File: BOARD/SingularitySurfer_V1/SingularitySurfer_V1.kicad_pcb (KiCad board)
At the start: 2 copper layers, 99.1 x 68.6 mm, 0 parts

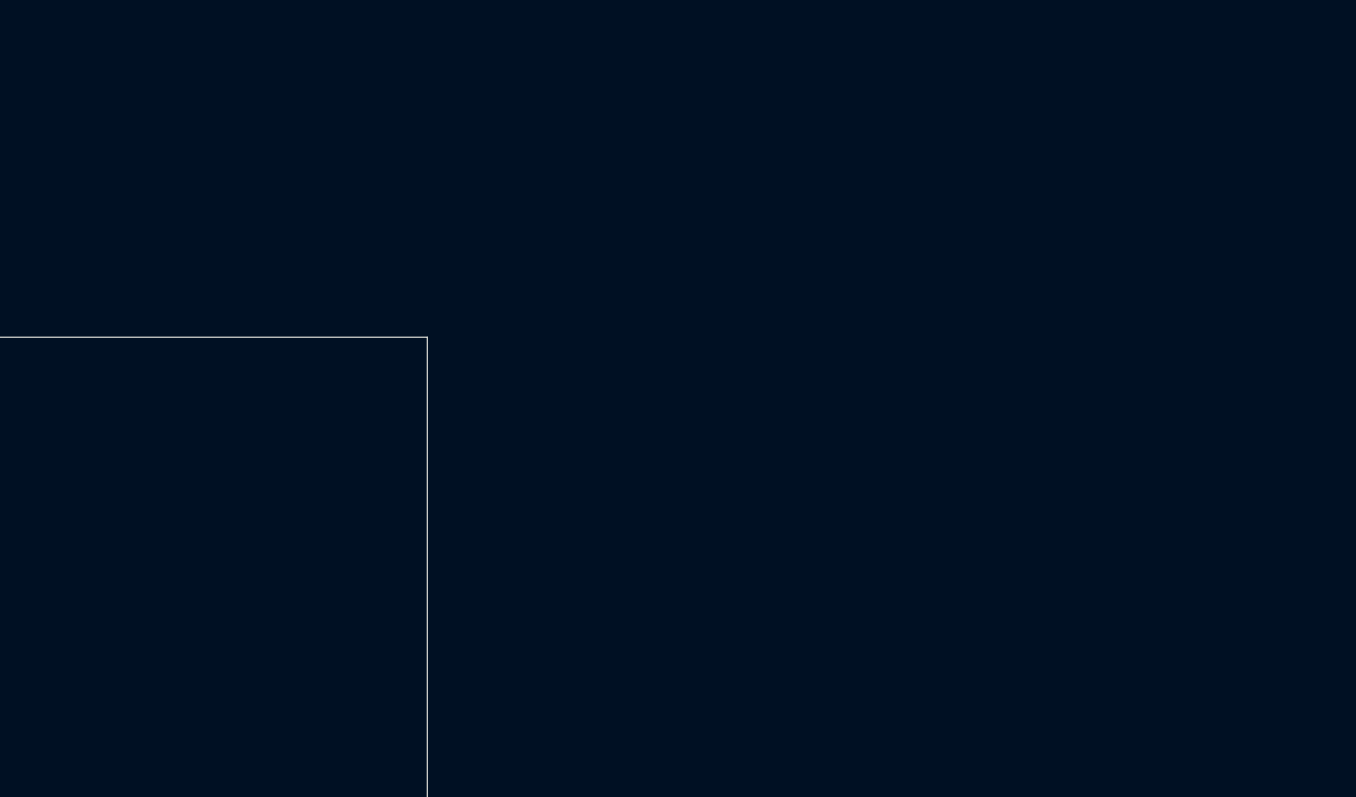
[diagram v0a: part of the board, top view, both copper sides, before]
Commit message: More work on final Schematic. Power, digital and output section close to final. No frontend yet.
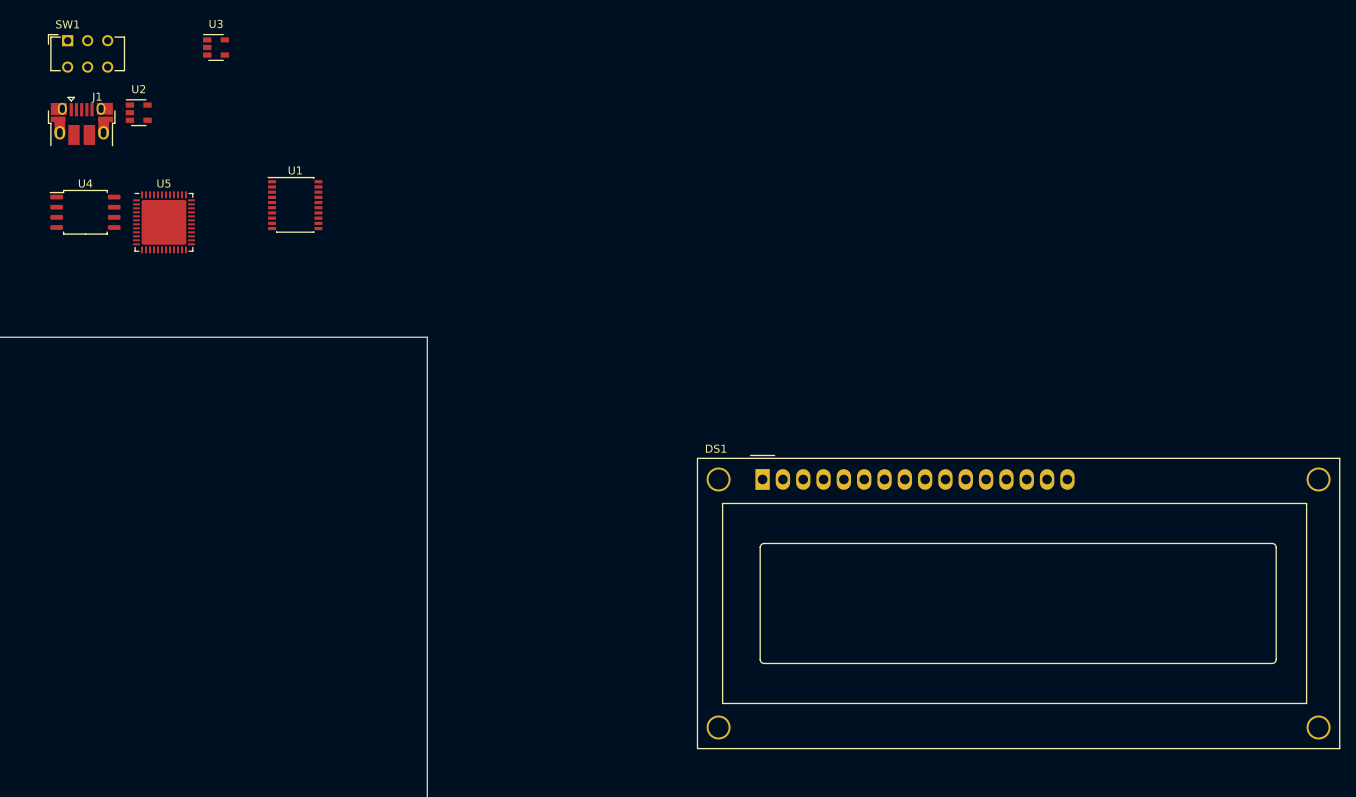
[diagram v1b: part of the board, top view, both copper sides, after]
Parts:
- added DS1: WC1602A, Display:WC1602A, F.Cu at (229.9, 81.3)
- added J1: USB_B_Micro, Connector_USB:USB_Micro-B_Amphenol_10103594-0001LF_Horizontal, F.Cu at (144.8, 36.8)
- added SW1: SW_DIP_x01, Button_Switch_THT:SW_CuK_JS202011AQN_DPDT_Angled, F.Cu at (143.0, 26.4)
- added U1: BD81870EFV, Package_SO:SSOP-20_4.4x6.5mm_P0.65mm, F.Cu at (171.4, 47.0)
- added U2: MIC5504-3.3YM5, Package_TO_SOT_SMD:SOT-23-5, F.Cu at (151.9, 35.4)
- added U3: TLV70212_SOT23-5, Package_TO_SOT_SMD:SOT-23-5, F.Cu at (161.6, 27.3)
- added U4: W25Q32JVSS, Package_SO:SOIC-8_5.23x5.23mm_P1.27mm, F.Cu at (145.2, 47.9)
- added U5: ICE40UP5K-SG48ITR, Package_DFN_QFN:QFN-48-1EP_7x7mm_P0.5mm_EP5.6x5.6mm, F.Cu at (155.0, 49.1)

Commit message: Final Board schematic almost done and started on layout
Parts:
- added  : MountingHole_4.3mm_M4_DIN965_Pad, MountingHole:MountingHole_4.3mm_M4_DIN965_Pad, F.Cu at (132.0, 53.0)
- added  : MountingHole_4.3mm_M4_DIN965_Pad, MountingHole:MountingHole_4.3mm_M4_DIN965_Pad, F.Cu at (29.0, 54.0)
- added  : MountingHole_4.3mm_M4_DIN965_Pad, MountingHole:MountingHole_4.3mm_M4_DIN965_Pad, F.Cu at (28.0, 135.0)
- added  : MountingHole_4.3mm_M4_DIN965_Pad, MountingHole:MountingHole_4.3mm_M4_DIN965_Pad, F.Cu at (132.0, 135.0)
- added +1: SW_Push, Button_Switch_THT:SW_PUSH-12mm, F.Cu at (124.0, 150.0)
- added -1: SW_Push, Button_Switch_THT:SW_PUSH-12mm, F.Cu at (124.0, 170.0)
- added C1: C, Capacitor_SMD:C_1206_3216Metric_Pad1.42x1.75mm_HandSolder, F.Cu at (68.3, 82.7)
- added C10: C, Capacitor_SMD:C_0805_2012Metric_Pad1.15x1.40mm_HandSolder, F.Cu at (85.9, 77.0)
- added C11: C, Capacitor_SMD:C_0805_2012Metric_Pad1.15x1.40mm_HandSolder, F.Cu at (88.4, 91.7)
- added C12: C, Capacitor_SMD:C_0805_2012Metric_Pad1.15x1.40mm_HandSolder, F.Cu at (87.9, 79.9)
- added C13: C, Capacitor_SMD:C_0805_2012Metric_Pad1.15x1.40mm_HandSolder, F.Cu at (92.4, 88.8)
- added C14: C, Capacitor_SMD:C_0805_2012Metric_Pad1.15x1.40mm_HandSolder, F.Cu at (83.6, 97.6)
- added C15: C, Capacitor_SMD:C_0805_2012Metric_Pad1.15x1.40mm_HandSolder, F.Cu at (83.6, 94.7)
- added C16: C, Capacitor_SMD:C_0805_2012Metric_Pad1.15x1.40mm_HandSolder, F.Cu at (92.6, 85.8)
- added C17: C, Capacitor_SMD:C_0805_2012Metric_Pad1.15x1.40mm_HandSolder, F.Cu at (97.4, 79.9)
- added C18: C, Capacitor_SMD:C_0805_2012Metric_Pad1.15x1.40mm_HandSolder, F.Cu at (83.6, 91.7)
- added C19: C, Capacitor_SMD:C_1206_3216Metric_Pad1.42x1.75mm_HandSolder, F.Cu at (66.4, 104.6)
- added C2: C, Capacitor_SMD:C_0805_2012Metric_Pad1.15x1.40mm_HandSolder, F.Cu at (67.4, 89.1)
- added C20: C, Capacitor_SMD:C_1206_3216Metric_Pad1.42x1.75mm_HandSolder, F.Cu at (60.5, 104.6)
- added C21: C, Capacitor_SMD:C_1206_3216Metric_Pad1.42x1.75mm_HandSolder, F.Cu at (60.5, 114.5)
- added C22: C, Capacitor_SMD:C_1206_3216Metric_Pad1.42x1.75mm_HandSolder, F.Cu at (72.4, 104.6)
- added C23: C, Capacitor_SMD:C_1206_3216Metric_Pad1.42x1.75mm_HandSolder, F.Cu at (66.4, 107.9)
- added C24: C, Capacitor_SMD:C_1206_3216Metric_Pad1.42x1.75mm_HandSolder, F.Cu at (60.5, 111.2)
- added C25: C, Capacitor_SMD:C_1206_3216Metric_Pad1.42x1.75mm_HandSolder, F.Cu at (60.5, 107.9)
- added C26: C, Capacitor_SMD:C_0805_2012Metric_Pad1.15x1.40mm_HandSolder, F.Cu at (92.6, 82.9)
- added C27: C, Capacitor_SMD:C_0805_2012Metric_Pad1.15x1.40mm_HandSolder, F.Cu at (87.6, 88.8)
- added C28: C, Capacitor_SMD:C_0805_2012Metric_Pad1.15x1.40mm_HandSolder, F.Cu at (78.9, 98.0)
- added C29: C, Capacitor_SMD:C_0805_2012Metric_Pad1.15x1.40mm_HandSolder, F.Cu at (97.4, 82.9)
- added C3: C, Capacitor_SMD:C_0805_2012Metric_Pad1.15x1.40mm_HandSolder, F.Cu at (73.6, 82.5)
- added C30: C, Capacitor_SMD:C_0805_2012Metric_Pad1.15x1.40mm_HandSolder, F.Cu at (83.1, 82.9)
- added C31: C, Capacitor_SMD:C_0805_2012Metric_Pad1.15x1.40mm_HandSolder, F.Cu at (69.4, 98.0)
- added C32: C, Capacitor_SMD:C_0805_2012Metric_Pad1.15x1.40mm_HandSolder, F.Cu at (78.1, 89.1)
- added C33: 10u, Capacitor_SMD:C_0805_2012Metric_Pad1.15x1.40mm_HandSolder, F.Cu at (127.2, 104.2)
- added C34: 10u, Capacitor_SMD:C_0805_2012Metric_Pad1.15x1.40mm_HandSolder, F.Cu at (109.1, 113.2)
- added C35: 1u, Capacitor_SMD:C_1206_3216Metric_Pad1.42x1.75mm_HandSolder, F.Cu at (117.0, 105.4)
- added C36: C, Capacitor_SMD:C_1206_3216Metric_Pad1.42x1.75mm_HandSolder, F.Cu at (124.3, 94.9)
- added C37: C, Capacitor_SMD:C_1206_3216Metric_Pad1.42x1.75mm_HandSolder, F.Cu at (103.8, 110.8)
- added C38: C, Capacitor_SMD:C_1206_3216Metric_Pad1.42x1.75mm_HandSolder, F.Cu at (111.1, 110.1)
- added C39: C, Capacitor_SMD:C_1206_3216Metric_Pad1.42x1.75mm_HandSolder, F.Cu at (116.8, 102.1)
- added C4: C, Capacitor_SMD:C_1206_3216Metric_Pad1.42x1.75mm_HandSolder, F.Cu at (68.0, 86.0)
- added C40: C, Capacitor_SMD:C_1206_3216Metric_Pad1.42x1.75mm_HandSolder, F.Cu at (103.8, 114.1)
- added C41: C, Capacitor_SMD:C_1206_3216Metric_Pad1.42x1.75mm_HandSolder, F.Cu at (124.3, 98.2)
- added C42: C, Capacitor_SMD:C_1206_3216Metric_Pad1.42x1.75mm_HandSolder, F.Cu at (111.1, 106.8)
- added C43: C, Capacitor_SMD:C_1206_3216Metric_Pad1.42x1.75mm_HandSolder, F.Cu at (60.5, 91.3)
- added C44: C, Capacitor_SMD:C_0805_2012Metric_Pad1.15x1.40mm_HandSolder, F.Cu at (90.7, 77.0)
- added C45: C, Capacitor_SMD:C_0805_2012Metric_Pad1.15x1.40mm_HandSolder, F.Cu at (78.1, 86.2)
- added C46: C, Capacitor_SMD:C_0805_2012Metric_Pad1.15x1.40mm_HandSolder, F.Cu at (69.4, 95.0)
- added C47: C, Capacitor_SMD:C_0805_2012Metric_Pad1.15x1.40mm_HandSolder, F.Cu at (69.4, 92.1)
- added C48: C, Capacitor_SMD:C_0805_2012Metric_Pad1.15x1.40mm_HandSolder, F.Cu at (59.9, 97.3)
- added C49: C, Capacitor_SMD:C_0805_2012Metric_Pad1.15x1.40mm_HandSolder, F.Cu at (83.1, 79.9)
- added C5: C, Capacitor_SMD:C_0805_2012Metric_Pad1.15x1.40mm_HandSolder, F.Cu at (75.3, 114.0)
- added C50: C, Capacitor_SMD:C_0805_2012Metric_Pad1.15x1.40mm_HandSolder, F.Cu at (73.4, 88.8)
- added C51: C, Capacitor_SMD:C_1206_3216Metric_Pad1.42x1.75mm_HandSolder, F.Cu at (75.8, 77.1)
- added C52: C, Capacitor_SMD:C_0805_2012Metric_Pad1.15x1.40mm_HandSolder, F.Cu at (64.6, 97.3)
- added C53: C, Capacitor_SMD:C_0805_2012Metric_Pad1.15x1.40mm_HandSolder, F.Cu at (78.4, 83.2)
- added C54: C, Capacitor_SMD:C_0805_2012Metric_Pad1.15x1.40mm_HandSolder, F.Cu at (87.9, 85.8)
- added C55: C, Capacitor_SMD:C_0805_2012Metric_Pad1.15x1.40mm_HandSolder, F.Cu at (59.9, 94.4)
- added C56: C, Capacitor_SMD:C_0805_2012Metric_Pad1.15x1.40mm_HandSolder, F.Cu at (81.2, 77.0)
- added C6: C, Capacitor_SMD:C_0805_2012Metric_Pad1.15x1.40mm_HandSolder, F.Cu at (64.6, 94.4)
- added C7: C, Capacitor_SMD:C_0805_2012Metric_Pad1.15x1.40mm_HandSolder, F.Cu at (78.4, 80.3)
- added C8: C, Capacitor_SMD:C_0805_2012Metric_Pad1.15x1.40mm_HandSolder, F.Cu at (73.4, 85.8)
- added C9: C, Capacitor_SMD:C_0805_2012Metric_Pad1.15x1.40mm_HandSolder, F.Cu at (78.9, 95.0)
- added D1: D, Diode_SMD:D_2010_5025Metric_Pad1.52x2.65mm_HandSolder, F.Cu at (61.4, 77.6)
- added D10: D_Schottky_x2_Serial_AKC, Package_TO_SOT_SMD:SOT-23, F.Cu at (83.2, 118.6)
- added D11: D_Schottky_x2_Serial_AKC, Package_TO_SOT_SMD:SOT-23, F.Cu at (87.6, 118.6)
- added D12: LED, LED_SMD:LED_0805_2012Metric_Pad1.15x1.40mm_HandSolder, F.Cu at (33.0, 99.0)
- added D13: D_Zener, Diode_SMD:D_SOD-323, F.Cu at (122.8, 112.4)
- added D14: D_Schottky_x2_Serial_AKC, Package_TO_SOT_SMD:SOT-23, F.Cu at (118.5, 112.2)
- added D15: D_Schottky_x2_Serial_AKC, Package_TO_SOT_SMD:SOT-23, F.Cu at (125.8, 108.6)
- added D16: D_Zener, Diode_SMD:D_SOD-323, F.Cu at (92.9, 91.7)
- added D17: D_Schottky_x2_Serial_AKC, Package_TO_SOT_SMD:SOT-23, F.Cu at (88.2, 95.5)
- added D2: D, Diode_SMD:D_2010_5025Metric_Pad1.52x2.65mm_HandSolder, F.Cu at (61.4, 81.9)
- added D3: D, Diode_SMD:D_SOD-123F, F.Cu at (66.2, 111.2)
- added D3001: LED, LED_SMD:LED_0805_2012Metric_Pad1.15x1.40mm_HandSolder, F.Cu at (24.0, 88.0)
- added D4: D_Schottky_x2_Serial_AKC, Package_TO_SOT_SMD:SOT-23, F.Cu at (78.7, 117.7)
- added D5: LED, LED_SMD:LED_0805_2012Metric_Pad1.15x1.40mm_HandSolder, F.Cu at (94.0, 132.0)
- added D6: LED, LED_SMD:LED_0805_2012Metric_Pad1.15x1.40mm_HandSolder, F.Cu at (108.0, 132.0)
- added D7: LED, LED_SMD:LED_0805_2012Metric_Pad1.15x1.40mm_HandSolder, F.Cu at (101.0, 132.0)
- added D8: LED, LED_SMD:LED_0805_2012Metric_Pad1.15x1.40mm_HandSolder, F.Cu at (115.0, 132.0)
- added D9: D_Schottky_x2_Serial_AKC, Package_TO_SOT_SMD:SOT-23, F.Cu at (84.7, 114.1)
- added G***: LOGO, SingularitySurfer_Logo:SingularitySurfer_Logo, F.Cu at (105.0, 63.0)
- added J10: Conn_01x02, Connector_PinHeader_2.54mm:PinHeader_1x02_P2.54mm_Vertical, F.Cu at (111.5, 100.3)
- added J11: Conn_Coaxial, Connector_Coaxial:SMA_Molex_73251-2200_Horizontal, F.Cu at (120.0, 50.0)
- added J12: Conn_Coaxial, Connector_Coaxial:SMA_Molex_73251-2200_Horizontal, F.Cu at (85.0, 50.0)
- added J2: Conn_01x04_Male, Connector_PinHeader_1.27mm:PinHeader_1x04_P1.27mm_Vertical, F.Cu at (24.0, 119.0)
- added J3: Conn_Coaxial, Connector_Coaxial:SMA_Molex_73251-2200_Horizontal, F.Cu at (135.0, 65.0)
- added J4: Conn_Coaxial, Connector_Coaxial:SMA_Molex_73251-2200_Horizontal, F.Cu at (135.0, 85.0)
- added J5: Conn_Coaxial, Connector_Coaxial:SMA_Molex_73251-2200_Horizontal, F.Cu at (135.0, 105.0)
- added J6: Conn_Coaxial, Connector_Coaxial:SMA_Molex_73251-2200_Horizontal, F.Cu at (135.0, 125.0)
- added J7: Conn_01x12, Connector_PinHeader_1.27mm:PinHeader_1x12_P1.27mm_Vertical, F.Cu at (24.0, 98.4)
- added J8: Conn_01x02_Male, Connector_PinHeader_1.27mm:PinHeader_1x02_P1.27mm_Vertical, F.Cu at (105.0, 87.0)
- added J9: Conn_01x02, Connector_PinHeader_2.54mm:PinHeader_1x02_P2.54mm_Vertical, F.Cu at (119.0, 95.6)
- added L1: INDUCTOR, Inductor_SMD:L_Taiyo-Yuden_NR-40xx_HandSoldering, F.Cu at (69.1, 78.3)
- added L2: INDUCTOR, Inductor_SMD:L_Taiyo-Yuden_NR-40xx_HandSoldering, F.Cu at (61.3, 86.9)
- added MENU1: SW_Push, Button_Switch_THT:SW_PUSH-12mm, F.Cu at (36.0, 155.0)
- added R1: R, Resistor_SMD:R_0805_2012Metric_Pad1.15x1.40mm_HandSolder, F.Cu at (95.4, 77.0)
- added R10: R, Resistor_SMD:R_0805_2012Metric_Pad1.15x1.40mm_HandSolder, F.Cu at (71.8, 107.7)
- added R11: R, Resistor_SMD:R_0805_2012Metric_Pad1.15x1.40mm_HandSolder, F.Cu at (86.0, 107.4)
- added R12: R, Resistor_SMD:R_0805_2012Metric_Pad1.15x1.40mm_HandSolder, F.Cu at (80.1, 113.6)
- added R13: R, Resistor_SMD:R_0805_2012Metric_Pad1.15x1.40mm_HandSolder, F.Cu at (74.1, 120.3)
- added R14: R, Resistor_SMD:R_0805_2012Metric_Pad1.15x1.40mm_HandSolder, F.Cu at (86.0, 110.3)
- added R15: R, Resistor_SMD:R_0805_2012Metric_Pad1.15x1.40mm_HandSolder, F.Cu at (69.4, 120.3)
- added R16: R, Resistor_SMD:R_0805_2012Metric_Pad1.15x1.40mm_HandSolder, F.Cu at (65.8, 114.4)
- added R17: R, Resistor_SMD:R_0805_2012Metric_Pad1.15x1.40mm_HandSolder, F.Cu at (59.9, 117.6)
- added R18: R, Resistor_SMD:R_0805_2012Metric_Pad1.15x1.40mm_HandSolder, F.Cu at (77.7, 104.4)
- added R19: R, Resistor_SMD:R_0805_2012Metric_Pad1.15x1.40mm_HandSolder, F.Cu at (71.3, 111.0)
- added R2: R, Resistor_SMD:R_0805_2012Metric_Pad1.15x1.40mm_HandSolder, F.Cu at (74.1, 98.0)
- added R20: R, Resistor_SMD:R_0805_2012Metric_Pad1.15x1.40mm_HandSolder, F.Cu at (64.6, 117.6)
- added R21: R, Resistor_SMD:R_0805_2012Metric_Pad1.15x1.40mm_HandSolder, F.Cu at (76.5, 107.7)
- added R22: R, Resistor_SMD:R_0805_2012Metric_Pad1.15x1.40mm_HandSolder, F.Cu at (70.6, 114.4)
- added R23: R, Resistor_SMD:R_0805_2012Metric_Pad1.15x1.40mm_HandSolder, F.Cu at (82.5, 104.4)
- added R24: R, Resistor_SMD:R_0805_2012Metric_Pad1.15x1.40mm_HandSolder, F.Cu at (76.1, 110.7)
- added R25: R, Resistor_SMD:R_0805_2012Metric_Pad1.15x1.40mm_HandSolder, F.Cu at (69.4, 117.3)
- added R26: R, Resistor_SMD:R_0805_2012Metric_Pad1.15x1.40mm_HandSolder, F.Cu at (81.3, 107.4)
- added R27: R, Resistor_SMD:R_0805_2012Metric_Pad1.15x1.40mm_HandSolder, F.Cu at (121.2, 108.5)
- added R28: R, Resistor_SMD:R_0805_2012Metric_Pad1.15x1.40mm_HandSolder, F.Cu at (127.0, 101.3)
- added R29: R, Resistor_SMD:R_0805_2012Metric_Pad1.15x1.40mm_HandSolder, F.Cu at (129.7, 94.7)
- added R3: R, Resistor_SMD:R_0805_2012Metric_Pad1.15x1.40mm_HandSolder, F.Cu at (82.9, 88.8)
- added R30: R, Resistor_SMD:R_0805_2012Metric_Pad1.15x1.40mm_HandSolder, F.Cu at (122.2, 101.9)
- added R31: R, Resistor_SMD:R_0805_2012Metric_Pad1.15x1.40mm_HandSolder, F.Cu at (116.5, 108.5)
- added R32: R, Resistor_SMD:R_0805_2012Metric_Pad1.15x1.40mm_HandSolder, F.Cu at (122.4, 104.9)
- added R33: R, Resistor_SMD:R_0805_2012Metric_Pad1.15x1.40mm_HandSolder, F.Cu at (129.7, 97.7)
- added R34: R, Resistor_SMD:R_0805_2012Metric_Pad1.15x1.40mm_HandSolder, F.Cu at (113.8, 113.2)
- added R35: R, Resistor_SMD:R_0805_2012Metric_Pad1.15x1.40mm_HandSolder, F.Cu at (74.1, 95.0)
- added R36: R, Resistor_SMD:R_0805_2012Metric_Pad1.15x1.40mm_HandSolder, F.Cu at (74.1, 92.1)
- added R37: R, Resistor_SMD:R_0805_2012Metric_Pad1.15x1.40mm_HandSolder, F.Cu at (97.4, 85.8)
- added R38: R, Resistor_SMD:R_0805_2012Metric_Pad1.15x1.40mm_HandSolder, F.Cu at (83.1, 85.8)
- added R4: R, Resistor_SMD:R_0805_2012Metric_Pad1.15x1.40mm_HandSolder, F.Cu at (78.9, 92.1)
- added R5: R, Resistor_SMD:R_0805_2012Metric_Pad1.15x1.40mm_HandSolder, F.Cu at (87.9, 82.9)
- added R6: R, Resistor_SMD:R_0805_2012Metric_Pad1.15x1.40mm_HandSolder, F.Cu at (92.6, 79.9)
- added R7: R, Resistor_SMD:R_0805_2012Metric_Pad1.15x1.40mm_HandSolder, F.Cu at (87.2, 104.4)
- added R8: R, Resistor_SMD:R_0805_2012Metric_Pad1.15x1.40mm_HandSolder, F.Cu at (81.3, 110.3)
- added R9: R, Resistor_SMD:R_0805_2012Metric_Pad1.15x1.40mm_HandSolder, F.Cu at (74.1, 117.3)
- added SET1001: SW_Push, Button_Switch_THT:SW_PUSH-12mm, F.Cu at (36.0, 175.0)
- added SW6: SW_Push, Button_Switch_THT:SW_PUSH_6mm, F.Cu at (30.0, 103.0)
- added U10: REF5050AD, Package_SO:SOIC-8_3.9x4.9mm_P1.27mm, F.Cu at (105.0, 96.5)
- added U11: AD8675, Package_SO:MSOP-8_3x3mm_P0.65mm, F.Cu at (113.0, 95.6)
- added U12: AD8253, Package_SO:MSOP-10_3x3mm_P0.5mm, F.Cu at (104.5, 102.1)
- added U13: LT3032, Package_DFN_QFN:Linear_DE14MA, F.Cu at (123.4, 76.3)
- added U14: AP2114-1.8, Package_TO_SOT_SMD:TO-252-3_TabPin2, F.Cu at (43.0, 52.0)
- added U6: 74LVC1G17, Package_TO_SOT_SMD:SOT-23-5_HandSoldering, F.Cu at (72.6, 109.1)
- added U7: OPA1679, Package_SO:SOIC-14_3.9x8.7mm_P1.27mm, F.Cu at (91.0, 100.0)
- added U9: MCP33131D, Package_SO:MSOP-10_3x3mm_P0.5mm, F.Cu at (104.5, 106.8)
- added X1: DFA-S11, Oscillator:Oscillator_SMD_Fordahl_DFAS11-4Pin_7.0x5.0mm, F.Cu at (75.3, 117.7)
- U2, U3: footprint Package_TO_SOT_SMD:SOT-23-5 -> Package_TO_SOT_SMD:SOT-23-5_HandSoldering
- moved DS1 193.4 mm to (48.0, 147.0)
- moved U1 136.0 mm to (38.0, 73.0)
- moved U4 130.2 mm to (41.0, 126.0)
- moved SW1 128.4 mm to (25.0, 77.0), turned to 270 degrees
- moved J1 125.6 mm to (23.2, 68.3), turned to 270 degrees
- moved U5 123.7 mm to (51.0, 116.0)
- moved U3 98.3 mm to (65.5, 48.3)
- moved U2 98.3 mm to (55.9, 56.4)
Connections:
- net Net-(C10-Pad2) renamed 5V
- DS1 pad 16: Net-(DS1-Pad16) -> GND
- U1 pad 9: VNEG -> Net-(C14-Pad2)
- U4 pad 8: Net-(U4-Pad8) -> 3V3
- U5 pad 22: Net-(U5-Pad22) -> 3V3
- U5 pad 25: Net-(U5-Pad25) -> Net-(DS1-Pad14)
- U5 pad 26: Net-(U5-Pad26) -> Net-(DS1-Pad13)
- U5 pad 27: Net-(U5-Pad27) -> Net-(DS1-Pad12)
- U5 pad 28: Net-(U5-Pad28) -> Net-(DS1-Pad11)
- U5 pad 31: Net-(U5-Pad31) -> Net-(DS1-Pad4)
- U5 pad 32: Net-(U5-Pad32) -> Net-(DS1-Pad5)
- U5 pad 34: Net-(U5-Pad34) -> Net-(DS1-Pad6)
- U5 pad 38: Net-(U5-Pad38) -> A0
- U5 pad 39: Net-(U5-Pad39) -> A1
- U5 pad 40: Net-(U5-Pad40) -> SCLK
- U5 pad 41: Net-(U5-Pad41) -> CONVST
- U5 pad 42: Net-(U5-Pad42) -> SDI
- U5 pad 43: Net-(U5-Pad43) -> SDO
- U5 pad 7: Net-(U5-Pad7) -> CDONE
- U5 pad 8: Net-(U5-Pad8) -> nCRESET
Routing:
- added copper zone on F.Cu, net GND
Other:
- board size 99.1 x 68.6 mm -> 120 x 140 mm
- board text added: "+"
- board text added: "-"
- board text added: "MENU"
- board text added: "SET"

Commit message: SignularitiSurfer final boar almost donegit status! Fuuuak this is getting rediculous...
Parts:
- removed the   at (132.0, 53.0)
- removed the   at (29.0, 54.0)
- removed the   at (28.0, 135.0)
- removed the   at (132.0, 135.0)
- removed D3001, D5, D6, D7, D8: LED, LED_SMD:LED_0805_2012Metric_Pad1.15x1.40mm_HandSolder
- removed DS1: WC1602A, Display:WC1602A
- removed J2: Conn_01x04_Male, Connector_PinHeader_1.27mm:PinHeader_1x04_P1.27mm_Vertical
- removed J6: Conn_Coaxial, Connector_Coaxial:SMA_Molex_73251-2200_Horizontal
- removed J7: Conn_01x12, Connector_PinHeader_1.27mm:PinHeader_1x12_P1.27mm_Vertical
- removed J8: Conn_01x02_Male, Connector_PinHeader_1.27mm:PinHeader_1x02_P1.27mm_Vertical
- removed SET1001: SW_Push, Button_Switch_THT:SW_PUSH-12mm
- removed SW6: SW_Push, Button_Switch_THT:SW_PUSH_6mm
- added  : TestPoint, TestPoint:TestPoint_Keystone_5000-5004_Miniature, F.Cu at (64.5, 65.5)
- added  : R, Resistor_SMD:R_0805_2012Metric_Pad1.15x1.40mm_HandSolder, F.Cu at (24.0, 86.0)
- added  : Conn_01x03, Connector_JST:JST_EH_B3B-EH-A_1x03_P2.50mm_Vertical, F.Cu at (131.0, 57.5)
- added  : TestPoint, TestPoint:TestPoint_Keystone_5000-5004_Miniature, F.Cu at (71.0, 90.5)
- added  : TestPoint, TestPoint:TestPoint_Keystone_5000-5004_Miniature, F.Cu at (85.8, 63.0)
- added  : TestPoint, TestPoint:TestPoint_Keystone_5000-5004_Miniature, F.Cu at (71.2, 53.0)
- added  : TestPoint, TestPoint:TestPoint_Keystone_5000-5004_Miniature, F.Cu at (86.2, 79.2)
- added  : TestPoint, TestPoint:TestPoint_Keystone_5000-5004_Miniature, F.Cu at (89.0, 83.0)
- added  : TestPoint, TestPoint:TestPoint_Keystone_5000-5004_Miniature, F.Cu at (29.2, 61.6)
- added  : TestPoint, TestPoint:TestPoint_Keystone_5000-5004_Miniature, F.Cu at (37.2, 58.0)
- added  : LED, LED_SMD:LED_0805_2012Metric_Pad1.15x1.40mm_HandSolder, F.Cu at (24.0, 89.0)
- added  : MountingHole_2.2mm_M2_DIN965_Pad, MountingHole:MountingHole_2.2mm_M2_DIN965_Pad, F.Cu at (134.0, 154.0)
- added  : LED, LED_SMD:LED_0805_2012Metric_Pad1.15x1.40mm_HandSolder, F.Cu at (121.0, 133.0)
- added  : LED, LED_SMD:LED_0805_2012Metric_Pad1.15x1.40mm_HandSolder, F.Cu at (111.0, 133.0)
- added  : LED, LED_SMD:LED_0805_2012Metric_Pad1.15x1.40mm_HandSolder, F.Cu at (101.0, 133.0)
- added  : LED, LED_SMD:LED_0805_2012Metric_Pad1.15x1.40mm_HandSolder, F.Cu at (91.0, 133.0)
- added  : SW_Push, Button_Switch_THT:SW_PUSH_6mm, F.Cu at (40.0, 99.0)
- added  : MountingHole_2.2mm_M2_DIN965_Pad, MountingHole:MountingHole_2.2mm_M2_DIN965_Pad, F.Cu at (26.0, 154.0)
- added  : Conn_Coaxial, Connector_Coaxial:SMA_Molex_73251-2200_Horizontal, F.Cu at (135.0, 126.0)
- added  : WC1602A, Display:WC1602A, F.Cu at (48.0, 140.0)
- added  : MountingHole_2.2mm_M2_DIN965_Pad, MountingHole:MountingHole_2.2mm_M2_DIN965_Pad, F.Cu at (26.0, 51.0)
- added  : MountingHole_2.2mm_M2_DIN965_Pad, MountingHole:MountingHole_2.2mm_M2_DIN965_Pad, F.Cu at (134.0, 51.0)
- added  : Conn_01x02_Male, Connector_PinHeader_2.54mm:PinHeader_1x02_P2.54mm_Vertical, F.Cu at (40.5, 134.0)
- added  : Conn_01x12, Connector_PinHeader_2.54mm:PinHeader_1x12_P2.54mm_Vertical, F.Cu at (23.0, 126.5)
- added  : Conn_01x04_Male, Connector_PinHeader_2.54mm:PinHeader_1x04_P2.54mm_Vertical, F.Cu at (32.0, 119.0)
- added  : TestPoint, TestPoint:TestPoint_Keystone_5000-5004_Miniature, F.Cu at (55.0, 90.5)
- added C57: C, Capacitor_SMD:C_0805_2012Metric_Pad1.15x1.40mm_HandSolder, F.Cu at (49.2, 54.0)
- added C58: C, Capacitor_SMD:C_0805_2012Metric_Pad1.15x1.40mm_HandSolder, F.Cu at (60.0, 87.5)
- added C59: C, Capacitor_SMD:C_0805_2012Metric_Pad1.15x1.40mm_HandSolder, F.Cu at (101.5, 106.0)
- added C60: C, Capacitor_SMD:C_0805_2012Metric_Pad1.15x1.40mm_HandSolder, F.Cu at (106.2, 106.0)
- added C61: C, Capacitor_SMD:C_0402_1005Metric, F.Cu at (60.0, 115.0)
- added C62: C, Capacitor_SMD:C_0402_1005Metric, F.Cu at (68.0, 106.0)
- added C63: C, Capacitor_SMD:C_0402_1005Metric, F.Cu at (74.5, 107.0)
- added C64: C, Capacitor_SMD:C_0805_2012Metric_Pad1.15x1.40mm_HandSolder, F.Cu at (113.5, 101.8)
- added G***: LOGO, SingularitySurfer_Logo:radiation, F.Cu at (117.8, 118.8)
- added J13: Conn_01x03, Connector_JST:JST_EH_B3B-EH-A_1x03_P2.50mm_Vertical, F.Cu at (131.0, 62.5)
- added REF**: OSHW-Logo2_14.6x12mm_SilkScreen, Symbol:OSHW-Logo2_14.6x12mm_SilkScreen, F.Cu at (117.8, 108.0)
- added SET1: SW_Push, Button_Switch_THT:SW_PUSH-12mm, F.Cu at (36.0, 167.0)
-  : renamed from D12
-  : renamed from J12
-  : renamed from J11
-  : renamed from J10
-  : renamed from J9
-  : renamed from J5
-  : renamed from J4
-  : renamed from J3
-  : renamed from SW1
- C30, C52: footprint Capacitor_SMD:C_0805_2012Metric_Pad1.15x1.40mm_HandSolder -> Capacitor_SMD:C_0402_1005Metric
- U13: footprint Package_DFN_QFN:Linear_DE14MA -> SingularitySurfer:DFN-14-1EP_split_bottom_pad_3x4mm_P0.5mm_EP1.7x3.3mm
- U5: footprint Package_DFN_QFN:QFN-48-1EP_7x7mm_P0.5mm_EP5.6x5.6mm -> SingularitySurfer:QFN-48-1EP_7x7mm_P0.5mm_EP5.6x5.6mm
- moved R7 78.3 mm to (126.0, 172.5), turned to 180 degrees
- moved R10 74.7 mm to (34.5, 172.5)
- moved C55 74.5 mm to (126.0, 60.0)
- moved C29 69.8 mm to (32.0, 107.5)
- moved C48 66.1 mm to (125.0, 86.0), turned to 90 degrees
- moved R9 64.8 mm to (136.5, 135.0), turned to 180 degrees
- moved R34 64.0 mm to (100.0, 50.8)
- moved R17 63.8 mm to (121.0, 136.0), turned to 180 degrees
- moved R8 63.2 mm to (22.5, 133.5), turned to 90 degrees
- moved D16 61.2 mm to (33.4, 77.4)
- moved D17 59.2 mm to (29.6, 87.4), turned to 90 degrees
- moved C50 59.0 mm to (126.0, 62.0)
- moved R2 58.7 mm to (41.8, 49.0), turned to 90 degrees
- moved R33 58.1 mm to (100.0, 47.8)
- moved R1 57.0 mm to (43.2, 54.0), turned to 90 degrees
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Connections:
- net Net-(C14-Pad2) renamed /Power/VNEG
-   pad 1: Net-(J5-Pad1) -> Net-(D9-Pad3)
-   pad 1: Net-(J4-Pad1) -> Net-(D11-Pad3)
- C45 pad 1: A1V8 -> 1V8
- C47 pad 1: A1V8 -> 1V8
- C52 pad 1: -8V -> 1V2
- D17 pad 3: Net-(D17-Pad3) -> 5V
- R37 pad 2: Net-(R37-Pad2) -> -8V
- U10 pad 2: +15V -> +8V
- U11 pad 4: -15V -> -8V
- U11 pad 7: +15V -> +8V
- U14 pad 3: A1V8 -> 1V8
- U6 pad 5: 5V -> 3V3
- U7 pad 1: Net-(J5-Pad1) -> Net-(D9-Pad3)
- U7 pad 13: Net-(J4-Pad1) -> Net-(D11-Pad3)
- U7 pad 14: Net-(J4-Pad1) -> Net-(D11-Pad3)
- U7 pad 2: Net-(J5-Pad1) -> Net-(D9-Pad3)
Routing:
- net 3V3: track 0.00 -> 444.0 mm, vias 0 -> 7
- net 5V: track 0.00 -> 355.4 mm, vias 0 -> 10
- net -8V: track 0.00 -> 201.8 mm, vias 0 -> 4
- net Net-(R10-Pad1): track 0.00 -> 169.5 mm, vias 0 -> 1
- net +8V: track 0.00 -> 169.2 mm, vias 0 -> 5
- net Net-(MENU1-Pad1): track 0.00 -> 152.6 mm, vias 0 -> 1
- net Net-(-1-Pad1): track 0.00 -> 122.9 mm, vias 0 -> 1
- net 1V2: track 0.00 -> 114.2 mm, vias 0 -> 2
- net Net-(+1-Pad1): track 0.00 -> 106.2 mm, vias 0 -> 3
- net A0: track 0.00 -> 78.9 mm, vias 0 -> 4
- net A1: track 0.00 -> 76.5 mm, vias 0 -> 4
- net Net-(U5-Pad23): track 0.00 -> 72.2 mm, vias 0 -> 2
- net Net-(R17-Pad2): track 0.00 -> 63.1 mm, vias 0 -> 2
- net Net-(C33-Pad1): track 0.00 -> 62.7 mm, vias 0 -> 2
- net Net-(DS1-Pad15): track 0.00 -> 61.1 mm, vias 0 -> 1
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- added copper zone on F.Cu, net /Power/VNEG
- added copper zone on F.Cu, net 5V
- added copper zone on B.Cu, net GND
- added copper zone on F.Cu, net Net-(D1-Pad2)
- added copper zone on F.Cu, net Net-(D2-Pad1)
- added copper zone on F.Cu, net Net-(L1-Pad2)
- added copper zone on F.Cu, net VPOS
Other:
- board size 120 x 140 mm -> 120 x 130 mm
- board text added: "+8V"
- board text added: "-8V"
- board text added: "1V2"
- board text added: "1V8"
- board text added: "3V3"
- board text added: "5V USB"
- board text added: "Backlight"
- board text added: "Clipping"
- board text added: "Done"
- board text added: "FPGA Lock-In Amplifier"
- board text added: "GND"
- board text added: "High EMI Emmitions"
- board text added: "ICE40UP5K"
- board text added: "IO"
- board text added: "IO10"
- board text added: "IO11"
- board text added: "IO12"
- board text added: "IO13"
- board text added: "IO18"
- board text added: "IO19"
- board text added: "IO20"
- board text added: "IO21"
- board text added: "IO9"
- board text added: "L1"
- board text added: "L2"
- board text added: "L3"
- board text added: "MISO"
- board text added: "MOSI"
- board text added: "Made by Humans on Earth"
- board text added: "OFF"
- board text added: "ON"
- board text added: "PREOUT"
- board text added: "Power"
- board text added: "Prog"
- board text added: "REFIN"
- board text added: "REFOUT"
- board text added: "Reset"
- board text added: "SCK"
- board text added: "SIGNAL"
- board text added: "SMA Center"
- board text added: "SMA Shield"
- board text added: "SS"
- board text added: "SingularitySurfer"
- board text added: "VNEG"
- board text added: "VPOS"
- board text added: "X/R"
- board text added: "Y/θ"

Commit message: Final board done, plotted and in production. Started on LCD driver, already working with scrolling HI :)
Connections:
-   pad 1: Net-(DS1-Pad1) -> GND
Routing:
- net /Power/VNEG: track 53.5 -> 54.6 mm
- net SDO: vias 3 -> 2
- net GND: vias 299 -> 313
- net (no net): vias 2 -> 0
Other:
- board text added: "VswNEG"
- board text added: "VswPOS"
- board text removed: "+8V"
- board text removed: "-8V"
